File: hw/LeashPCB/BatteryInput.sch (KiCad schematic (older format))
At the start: 13 parts

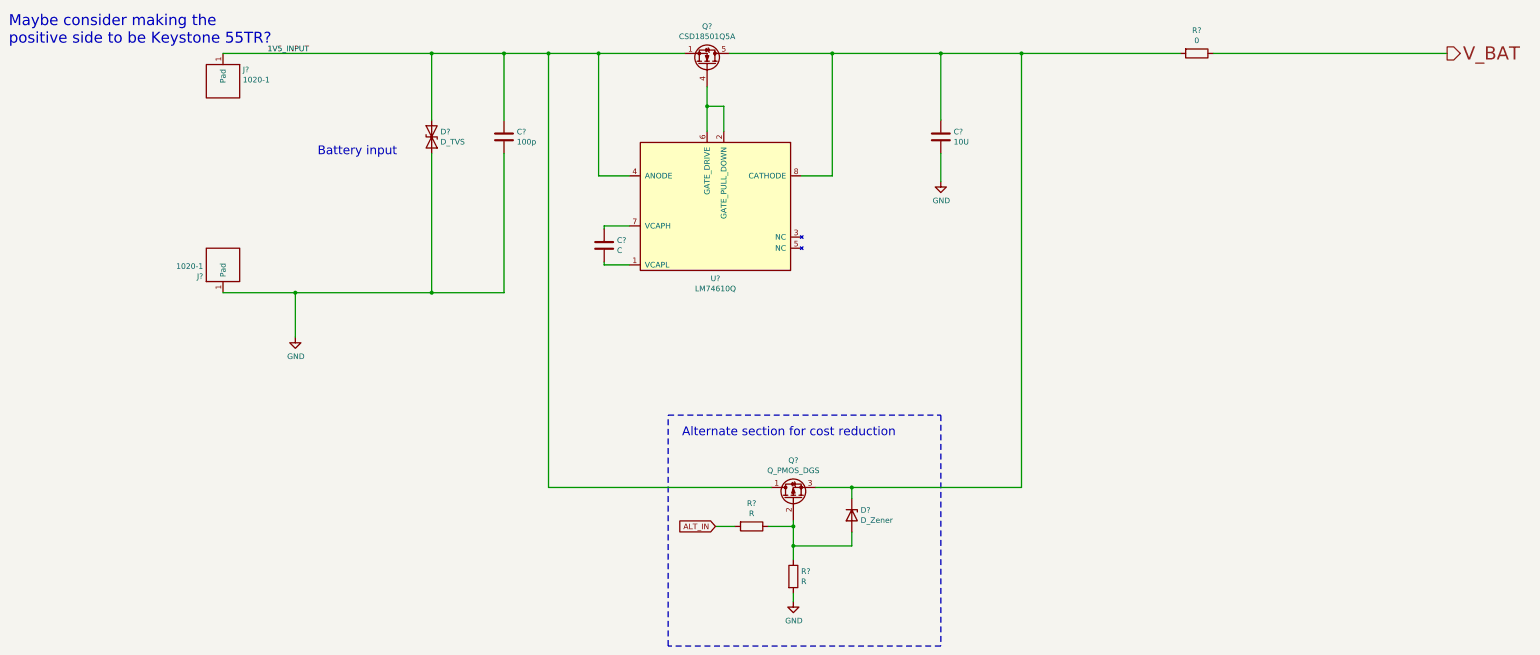
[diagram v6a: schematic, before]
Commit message: Shifted all components to the left on the layout and added passives
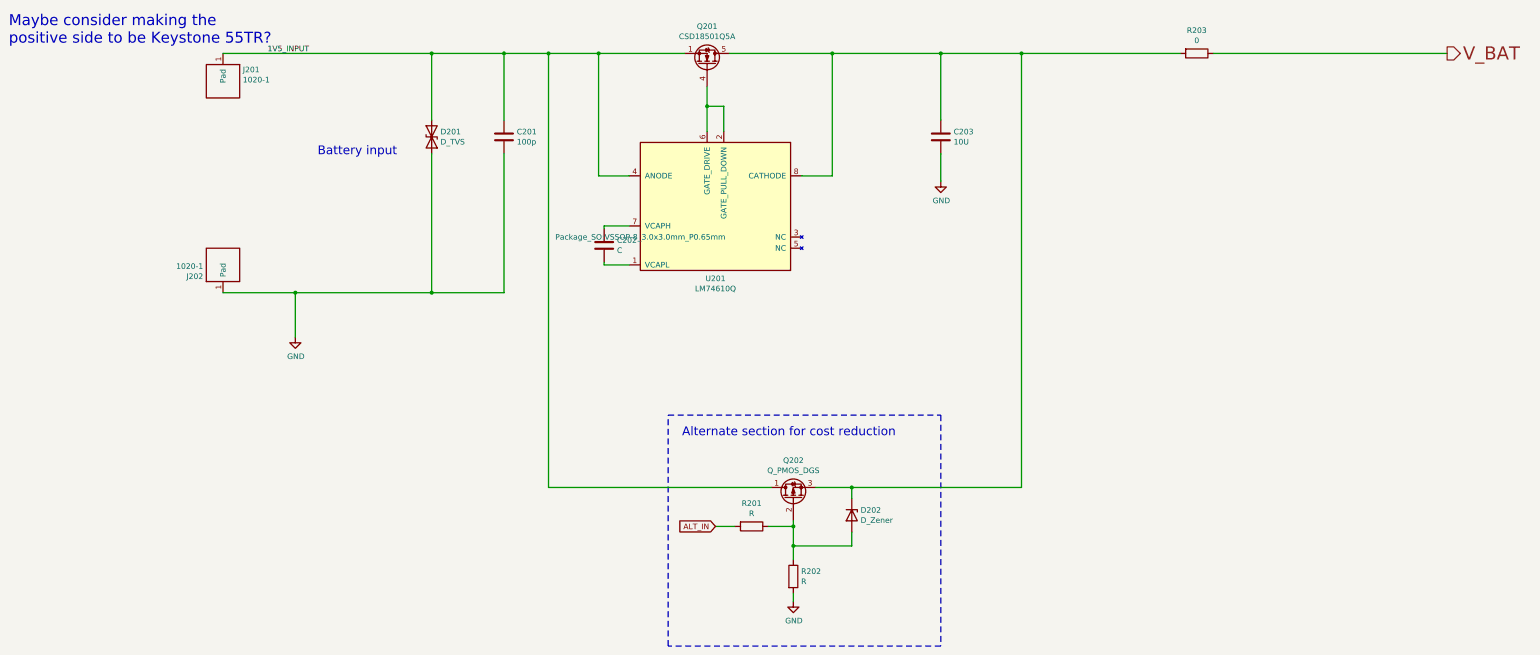
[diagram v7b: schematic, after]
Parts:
- C201, C202, C203: renamed from C?; footprint (none) -> Capacitor_SMD:C_0402_1005Metric
- R201, R202, R203: renamed from R?; footprint (none) -> Resistor_SMD:R_0402_1005Metric
- U201: renamed from U?; footprint (none) -> Package_SO:VSSOP-8_3.0x3.0mm_P0.65mm
- gave numbers to parts that had none: 6
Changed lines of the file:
@@
 	3150 2975 3150 3375
 $Comp
-L power:GND #PWR?
+L power:GND #PWR0101
 U 1 1 5D079C2D
 P 3150 3375
-F 0 "#PWR?" H 3150 3125 50  0001 C CNN
+F 0 "#PWR0101" H 3150 3125 50  0001 C CNN
 F 1 "GND" H 3155 3202 50  0000 C CNN
 F 2 "" H 3150 3375 50  0001 C CNN
@@
 	2500 2975 3150 2975
 $Comp
-L LeashPCB:1020-1 J?
+L LeashPCB:1020-1 J202
 U 1 1 5D079C36
 P 2500 2775
-F 0 "J?" V 2446 2953 50  0000 L CNN
+F 0 "J202" V 2446 2953 50  0000 L CNN
 F 1 "1020-1" V 2537 2953 50  0000 L CNN
 F 2 "leash:1020-1" H 2500 2775 50  0001 C CNN
@@
 $EndBitmap
 $Comp
-L LeashPCB:1020-1 J?
+L LeashPCB:1020-1 J201
 U 1 1 5D079C5E
 P 2500 1025
-F 0 "J?" V 2446 1203 50  0000 L CNN
+F 0 "J201" V 2446 1203 50  0000 L CNN
 F 1 "1020-1" V 2537 1203 50  0000 L CNN
 F 2 "leash:1020-1" H 2500 1025 50  0001 C CNN
@@
 1V5_INPUT
 $Comp
-L Device:D_TVS D?
+L Device:D_TVS D201
 U 1 1 5D067AEF
 P 4375 1575
-F 0 "D?" V 4329 1654 50  0000 L CNN
+F 0 "D201" V 4329 1654 50  0000 L CNN
 F 1 "D_TVS" V 4420 1654 50  0000 L CNN
 F 2 "" H 4375 1575 50  0001 C CNN
@@
 $EndComp
 $Comp
-L Device:C C?
+L Device:C C201
 U 1 1 5D067F64
 P 5025 1575
-F 0 "C?" H 5140 1621 50  0000 L CNN
+F 0 "C201" H 5140 1621 50  0000 L CNN
 F 1 "100p" H 5140 1530 50  0000 L CNN
-F 2 "" H 5063 1425 50  0001 C CNN
+F 2 "Capacitor_SMD:C_0402_1005Metric" H 5063 1425 50  0001 C CNN
 F 3 "~" H 5025 1575 50  0001 C CNN
 	1    5025 1575
@@
 $EndComp
 $Comp
-L Device:C C?
+L Device:C C202
 U 1 1 5D0681B7
 P 5925 2550
-F 0 "C?" H 6040 2596 50  0000 L CNN
+F 0 "C202" H 6040 2596 50  0000 L CNN
 F 1 "C" H 6040 2505 50  0000 L CNN
-F 2 "" H 5963 2400 50  0001 C CNN
+F 2 "Capacitor_SMD:C_0402_1005Metric" H 5963 2400 50  0001 C CNN
 F 3 "~" H 5925 2550 50  0001 C CNN
 	1    5925 2550
@@
 $EndComp
 $Comp
-L LeashPCB:LM74610QDGKRQ1 U?
+L LeashPCB:LM74610QDGKRQ1 U201
 U 1 1 5D069D70
 P 7000 2175
-F 0 "U?" H 6925 1502 50  0000 C CNN
+F 0 "U201" H 6925 1502 50  0000 C CNN
 F 1 "LM74610Q" H 6925 1411 50  0000 C CNN
-F 2 "" H 6250 1875 50  0001 C CNN
+F 2 "Package_SO:VSSOP-8_3.0x3.0mm_P0.65mm" H 6250 1875 50  0000 C CNN
 F 3 "http://www.ti.com/lit/ds/symlink/lm74610-q1.pdf" H 6250 1875 50  0001 C CNN
 F 4 "LM74610QDGKRQ1" H 7000 2175 50  0001 C CNN "MPN1"
@@
 	5925 2725 6150 2725
 $Comp
-L Device:C C?
+L Device:C C203
 U 1 1 5D06EB1F
 P 8950 1575
-F 0 "C?" H 9065 1621 50  0000 L CNN
+F 0 "C203" H 9065 1621 50  0000 L CNN
 F 1 "10U" H 9065 1530 50  0000 L CNN
-F 2 "" H 8988 1425 50  0001 C CNN
+F 2 "Capacitor_SMD:C_0402_1005Metric" H 8988 1425 50  0001 C CNN
 F 3 "~" H 8950 1575 50  0001 C CNN
 	1    8950 1575
@@
 	4375 2975 5025 2975
 $Comp
-L power:GND #PWR?
+L power:GND #PWR0102
 U 1 1 5D071998
 P 8950 1975
-F 0 "#PWR?" H 8950 1725 50  0001 C CNN
+F 0 "#PWR0102" H 8950 1725 50  0001 C CNN
 F 1 "GND" H 8955 1802 50  0000 C CNN
 F 2 "" H 8950 1975 50  0001 C CNN
@@
 $EndComp
 $Comp
-L Transistor_FET:CSD18501Q5A Q?
+L Transistor_FET:CSD18501Q5A Q201
 U 1 1 5D0747C0
 P 6850 925
-F 0 "Q?" V 7193 925 50  0000 C CNN
+F 0 "Q201" V 7193 925 50  0000 C CNN
 F 1 "CSD18501Q5A" V 7102 925 50  0000 C CNN
 F 2 "Package_TO_SOT_SMD:TDSON-8-1" H 7050 850 50  0001 L CIN
@@
 	5425 825  5025 825
 $Comp
-L Device:Q_PMOS_DGS Q?
+L Device:Q_PMOS_DGS Q202
 U 1 1 5D1B2FC4
 P 7625 4825
-F 0 "Q?" V 7968 4825 50  0000 C CNN
+F 0 "Q202" V 7968 4825 50  0000 C CNN
 F 1 "Q_PMOS_DGS" V 7877 4825 50  0000 C CNN
 F 2 "" H 7825 4925 50  0001 C CNN
@@
 $EndComp
 $Comp
-L Device:D_Zener D?
+L Device:D_Zener D202
 U 1 1 5D1B5E6D
 P 8150 4975
-F 0 "D?" V 8104 5054 50  0000 L CNN
+F 0 "D202" V 8104 5054 50  0000 L CNN
 F 1 "D_Zener" V 8195 5054 50  0000 L CNN
 F 2 "" H 8150 4975 50  0001 C CNN
@@
 $EndComp
 $Comp
-L Device:R R?
+L Device:R R202
 U 1 1 5D1B63DF
 P 7625 5525
-F 0 "R?" H 7695 5571 50  0000 L CNN
+F 0 "R202" H 7695 5571 50  0000 L CNN
 F 1 "R" H 7695 5480 50  0000 L CNN
-F 2 "" V 7555 5525 50  0001 C CNN
+F 2 "Resistor_SMD:R_0402_1005Metric" V 7555 5525 50  0001 C CNN
 F 3 "~" H 7625 5525 50  0001 C CNN
 	1    7625 5525
@@
 	7625 5250 7625 5375
 $Comp
-L power:GND #PWR?
+L power:GND #PWR0103
 U 1 1 5D1BC7E6
 P 7625 5750
-F 0 "#PWR?" H 7625 5500 50  0001 C CNN
+F 0 "#PWR0103" H 7625 5500 50  0001 C CNN
 F 1 "GND" H 7630 5577 50  0000 C CNN
 F 2 "" H 7625 5750 50  0001 C CNN
@@
 $EndComp
 $Comp
-L Device:R R?
+L Device:R R201
 U 1 1 5D1BDEB4
 P 7250 5075
-F 0 "R?" V 7043 5075 50  0000 C CNN
+F 0 "R201" V 7043 5075 50  0000 C CNN
 F 1 "R" V 7134 5075 50  0000 C CNN
-F 2 "" V 7180 5075 50  0001 C CNN
+F 2 "Resistor_SMD:R_0402_1005Metric" V 7180 5075 50  0001 C CNN
 F 3 "~" H 7250 5075 50  0001 C CNN
 	1    7250 5075
@@
 Alternate section for cost reduction
 $Comp
-L Device:R R?
+L Device:R R203
 U 1 1 5D1B1ECE
 P 11250 825
-F 0 "R?" V 11043 825 50  0000 C CNN
+F 0 "R203" V 11043 825 50  0000 C CNN
 F 1 "0" V 11134 825 50  0000 C CNN
-F 2 "" V 11180 825 50  0001 C CNN
+F 2 "Resistor_SMD:R_0402_1005Metric" V 11180 825 50  0001 C CNN
 F 3 "~" H 11250 825 50  0001 C CNN
 	1    11250 825

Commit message: Finished layout on the boost converters and enlarged the board slightly to allow for a larger battery and the large PCB antenna
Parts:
- added J203: 1076-1, leash:1020-1, symbol LeashPCB:1020-1
- J202: value 1020-1 -> 1076-1
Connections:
- net GND: now also J203.1 (Pad)
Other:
- note added: "Second pad for AA extension"
- note removed: "Maybe consider making the \npositive side to be Keystone 55TR?"
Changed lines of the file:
@@
 P 2500 2775
 F 0 "J202" V 2446 2953 50  0000 L CNN
-F 1 "1020-1" V 2537 2953 50  0000 L CNN
+F 1 "1076-1" V 2537 2953 50  0000 L CNN
 F 2 "leash:1020-1" H 2500 2775 50  0001 C CNN
 F 3 "" H 2500 2775 50  0001 C CNN
@@
 Wire Wire Line
 	11400 825  13500 825
-Text Notes 575  750  0    98   ~ 0
-Maybe consider making the \npositive side to be Keystone 55TR?
+Text Notes 1000 2575 0    50   ~ 0
+Second pad for AA extension
+$Comp
+L LeashPCB:1020-1 J203
+U 1 1 5D3D97E4
+P 1800 2775
+F 0 "J203" V 1746 2953 50  0000 L CNN
+F 1 "1076-1" V 1837 2953 50  0000 L CNN
+F 2 "leash:1020-1" H 1800 2775 50  0001 C CNN
+F 3 "" H 1800 2775 50  0001 C CNN
+F 4 "0.05" H 1800 2775 50  0001 C CNN "Standard Price"
+	1    1800 2775
+	0    -1   -1   0
+$EndComp
+Wire Wire Line
+	1800 2975 2500 2975
+Connection ~ 2500 2975
 $EndSCHEMATC
